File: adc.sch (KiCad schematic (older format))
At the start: 86 parts, among them J1 Conn_02x08_Odd_Even, J2 Conn_02x08_Odd_Even, J3 Conn_02x08_Odd_Even, J4 Conn_02x08_Odd_Even, J5 Conn_01x04_Male, J9 Conn_02x08_Odd_Even, U1 ADC128D818, U2 ADC128D818, U3 ADC128D818, U4 ADC128D818, U5 ADC128D818

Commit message: change tantalum cap footprint to Kemet C
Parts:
- C1, C10, C2, C5, C7, C9: footprint Capacitor_Tantalum_SMD:CP_EIA-3216-18_Kemet-A_Pad1.58x1.35mm_HandSolder -> Capacitor_Tantalum_SMD:CP_EIA-6032-28_Kemet-C_Pad2.25x2.35mm_HandSolder
- C13, C15, C17, C19: footprint Capacitor_Tantalum_SMD:CP_EIA-3528-12_Kemet-T_Pad1.50x2.35mm_HandSolder -> Capacitor_Tantalum_SMD:CP_EIA-6032-28_Kemet-C_Pad2.25x2.35mm_HandSolder
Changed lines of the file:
@@
 F 0 "C13" V 6650 5700 50  0000 L CNN
 F 1 "1U TANT C" V 6550 5400 50  0000 L CNN
-F 2 "Capacitor_Tantalum_SMD:CP_EIA-3528-12_Kemet-T_Pad1.50x2.35mm_HandSolder" H 6588 5900 50  0001 C CNN
+F 2 "Capacitor_Tantalum_SMD:CP_EIA-6032-28_Kemet-C_Pad2.25x2.35mm_HandSolder" H 6588 5900 50  0001 C CNN
 F 3 "~" H 6550 6050 50  0001 C CNN
 	1    6550 6050
@@
 F 0 "C9" H 4450 4300 50  0000 L CNN
 F 1 "1U TANT C" H 4400 4200 50  0000 L CNN
-F 2 "Capacitor_Tantalum_SMD:CP_EIA-3216-18_Kemet-A_Pad1.58x1.35mm_HandSolder" H 4938 4100 50  0001 C CNN
+F 2 "Capacitor_Tantalum_SMD:CP_EIA-6032-28_Kemet-C_Pad2.25x2.35mm_HandSolder" H 4938 4100 50  0001 C CNN
 F 3 "~" H 4900 4250 50  0001 C CNN
 	1    4900 4250
@@
 F 0 "C5" V 3100 6300 50  0000 L CNN
 F 1 "1U TANT C" V 3000 6000 50  0000 L CNN
-F 2 "Capacitor_Tantalum_SMD:CP_EIA-3216-18_Kemet-A_Pad1.58x1.35mm_HandSolder" H 3038 6500 50  0001 C CNN
+F 2 "Capacitor_Tantalum_SMD:CP_EIA-6032-28_Kemet-C_Pad2.25x2.35mm_HandSolder" H 3038 6500 50  0001 C CNN
 F 3 "~" H 3000 6650 50  0001 C CNN
 	1    3000 6650
@@
 F 0 "C1" H 900 4900 50  0000 L CNN
 F 1 "1U TANT C" H 850 4800 50  0000 L CNN
-F 2 "Capacitor_Tantalum_SMD:CP_EIA-3216-18_Kemet-A_Pad1.58x1.35mm_HandSolder" H 1388 4700 50  0001 C CNN
+F 2 "Capacitor_Tantalum_SMD:CP_EIA-6032-28_Kemet-C_Pad2.25x2.35mm_HandSolder" H 1388 4700 50  0001 C CNN
 F 3 "~" H 1350 4850 50  0001 C CNN
 	1    1350 4850
@@
 F 0 "C7" V 3500 2800 50  0000 L CNN
 F 1 "1U TANT C" V 3400 2500 50  0000 L CNN
-F 2 "Capacitor_Tantalum_SMD:CP_EIA-3216-18_Kemet-A_Pad1.58x1.35mm_HandSolder" H 3438 3000 50  0001 C CNN
+F 2 "Capacitor_Tantalum_SMD:CP_EIA-6032-28_Kemet-C_Pad2.25x2.35mm_HandSolder" H 3438 3000 50  0001 C CNN
 F 3 "~" H 3400 3150 50  0001 C CNN
 	1    3400 3150
@@
 F 0 "C2" H 1300 1400 50  0000 L CNN
 F 1 "1U TANT C" H 1250 1300 50  0000 L CNN
-F 2 "Capacitor_Tantalum_SMD:CP_EIA-3216-18_Kemet-A_Pad1.58x1.35mm_HandSolder" H 1788 1200 50  0001 C CNN
+F 2 "Capacitor_Tantalum_SMD:CP_EIA-6032-28_Kemet-C_Pad2.25x2.35mm_HandSolder" H 1788 1200 50  0001 C CNN
 F 3 "~" H 1750 1350 50  0001 C CNN
 	1    1750 1350
@@
 F 0 "C19" V 10200 2600 50  0000 L CNN
 F 1 "1U TANT C" V 10100 2300 50  0000 L CNN
-F 2 "Capacitor_Tantalum_SMD:CP_EIA-3528-12_Kemet-T_Pad1.50x2.35mm_HandSolder" H 10138 2800 50  0001 C CNN
+F 2 "Capacitor_Tantalum_SMD:CP_EIA-6032-28_Kemet-C_Pad2.25x2.35mm_HandSolder" H 10138 2800 50  0001 C CNN
 F 3 "~" H 10100 2950 50  0001 C CNN
 	1    10100 2950
@@
 F 0 "C17" H 8000 1200 50  0000 L CNN
 F 1 "1U TANT C" H 7950 1100 50  0000 L CNN
-F 2 "Capacitor_Tantalum_SMD:CP_EIA-3528-12_Kemet-T_Pad1.50x2.35mm_HandSolder" H 8488 1000 50  0001 C CNN
+F 2 "Capacitor_Tantalum_SMD:CP_EIA-6032-28_Kemet-C_Pad2.25x2.35mm_HandSolder" H 8488 1000 50  0001 C CNN
 F 3 "~" H 8450 1150 50  0001 C CNN
 	1    8450 1150
@@
 F 0 "C15" V 6950 2600 50  0000 L CNN
 F 1 "1U TANT C" V 6850 2300 50  0000 L CNN
-F 2 "Capacitor_Tantalum_SMD:CP_EIA-3528-12_Kemet-T_Pad1.50x2.35mm_HandSolder" H 6888 2800 50  0001 C CNN
+F 2 "Capacitor_Tantalum_SMD:CP_EIA-6032-28_Kemet-C_Pad2.25x2.35mm_HandSolder" H 6888 2800 50  0001 C CNN
 F 3 "~" H 6850 2950 50  0001 C CNN
 	1    6850 2950
@@
 F 0 "C10" H 4750 1200 50  0000 L CNN
 F 1 "1U TANT C" H 4700 1100 50  0000 L CNN
-F 2 "Capacitor_Tantalum_SMD:CP_EIA-3216-18_Kemet-A_Pad1.58x1.35mm_HandSolder" H 5238 1000 50  0001 C CNN
+F 2 "Capacitor_Tantalum_SMD:CP_EIA-6032-28_Kemet-C_Pad2.25x2.35mm_HandSolder" H 5238 1000 50  0001 C CNN
 F 3 "~" H 5200 1150 50  0001 C CNN
 	1    5200 1150

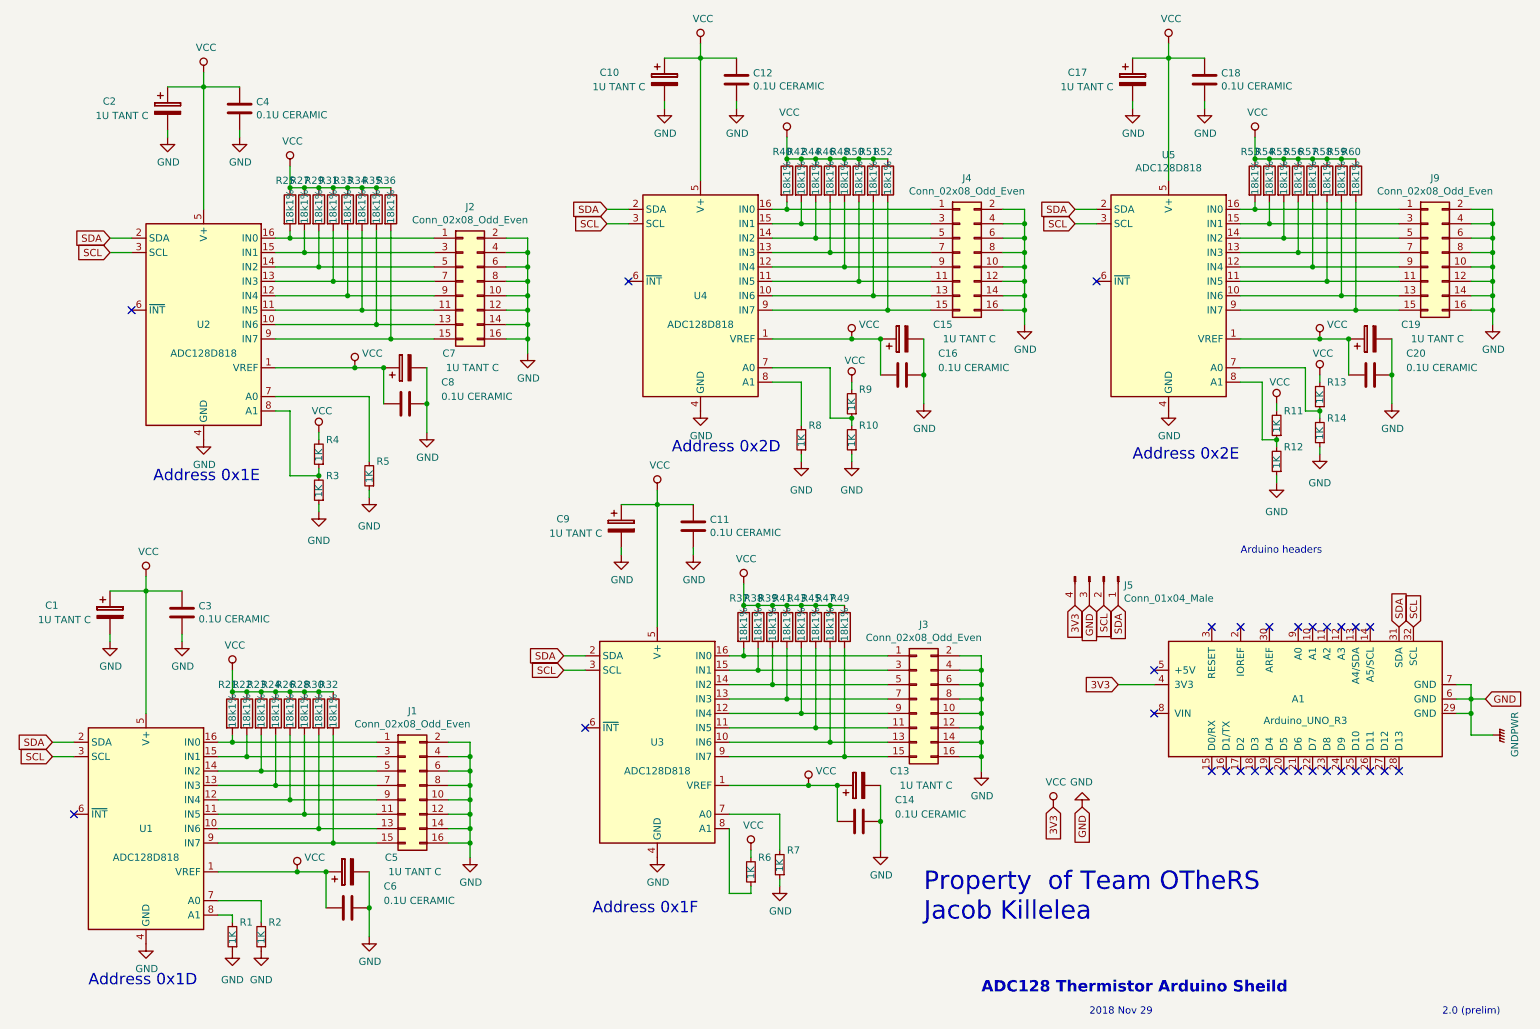
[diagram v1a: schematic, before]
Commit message: Replaced female 2x8 headers with male. Female makes more sense on the thermistors
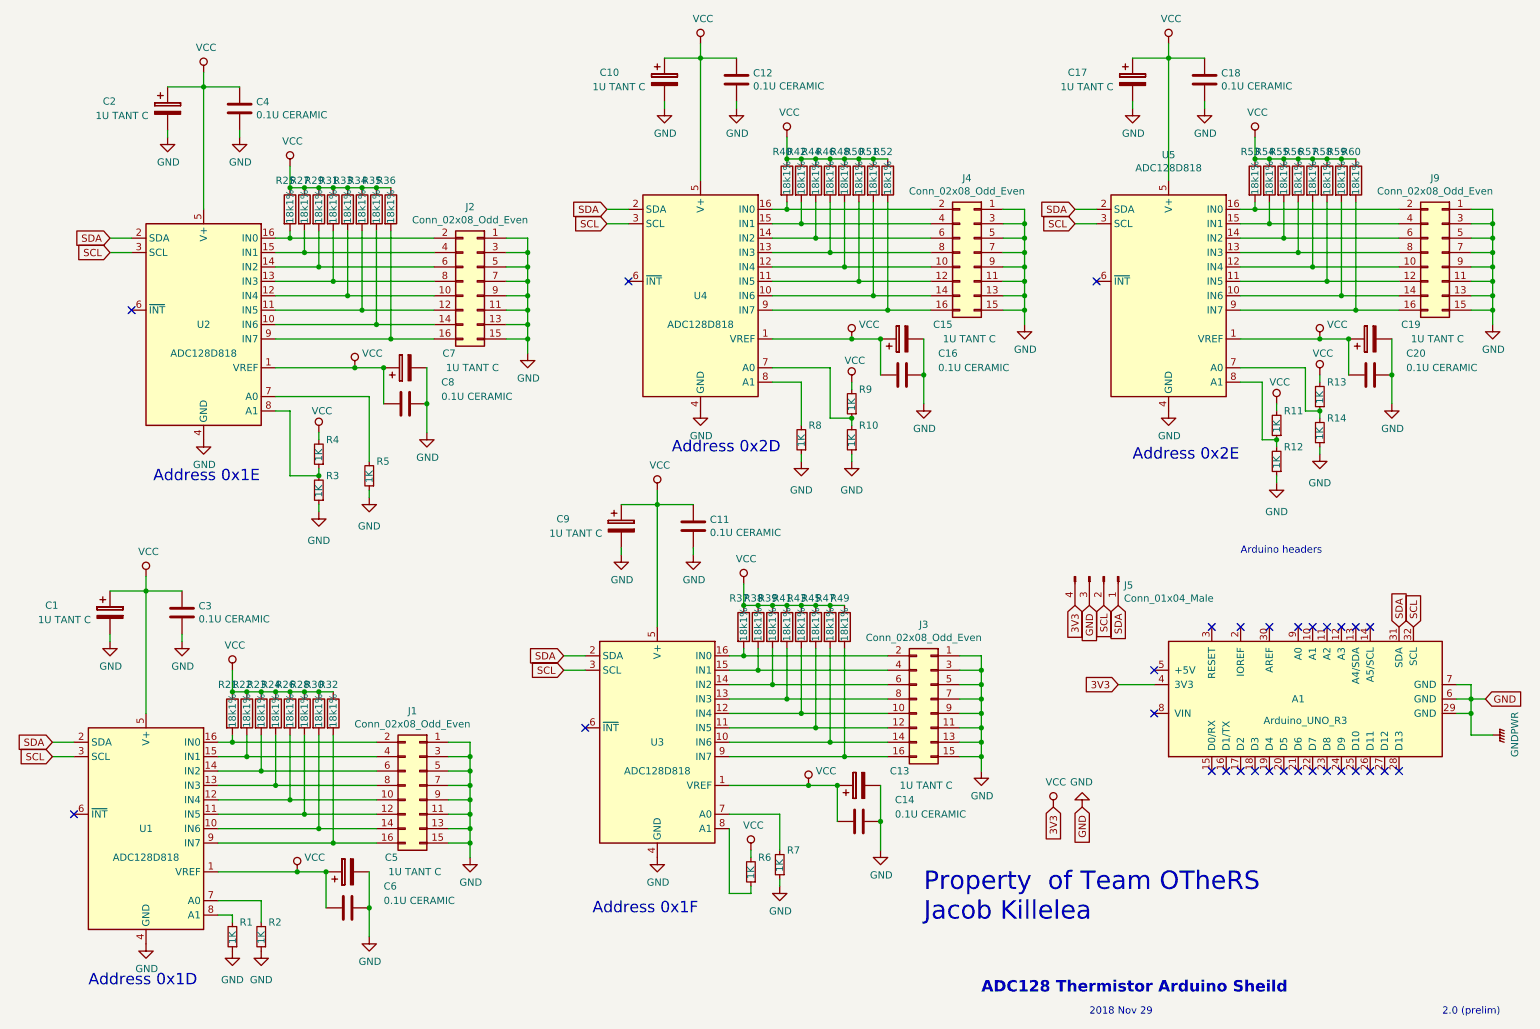
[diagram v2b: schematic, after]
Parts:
- J1, J2, J3, J4, J9: footprint Connector_PinSocket_2.54mm:PinSocket_2x08_P2.54mm_Vertical -> Connector_PinHeader_2.54mm:PinHeader_2x08_P2.54mm_Vertical
- J5: footprint Connector_PinSocket_2.54mm:PinSocket_1x04_P2.54mm_Vertical -> Connector_PinHeader_2.54mm:PinHeader_1x04_P2.54mm_Vertical
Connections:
- net GND: now also J1.1 (Pin_1), J1.11 (Pin_11), J1.13 (Pin_13), J1.15 (Pin_15), J1.3 (Pin_3), J1.5 (Pin_5), J1.7 (Pin_7), J1.9 (Pin_9), J2.1 (Pin_1), J2.11 (Pin_11), J2.13 (Pin_13), J2.15 (Pin_15), J2.3 (Pin_3), J2.5 (Pin_5), J2.7 (Pin_7), J2.9 (Pin_9), J3.1 (Pin_1), J3.11 (Pin_11), J3.13 (Pin_13), J3.15 (Pin_15), J3.3 (Pin_3), J3.5 (Pin_5), J3.7 (Pin_7), J3.9 (Pin_9), J4.1 (Pin_1), J4.11 (Pin_11), J4.13 (Pin_13), J4.15 (Pin_15), J4.3 (Pin_3), J4.5 (Pin_5), J4.7 (Pin_7), J4.9 (Pin_9), J9.1 (Pin_1), J9.11 (Pin_11), J9.13 (Pin_13), J9.15 (Pin_15), J9.3 (Pin_3), J9.5 (Pin_5), J9.7 (Pin_7), J9.9 (Pin_9); no longer J1.10 (Pin_10), J1.12 (Pin_12), J1.14 (Pin_14), J1.16 (Pin_16), J1.2 (Pin_2), J1.4 (Pin_4), J1.6 (Pin_6), J1.8 (Pin_8), J2.10 (Pin_10), J2.12 (Pin_12), J2.14 (Pin_14), J2.16 (Pin_16), J2.2 (Pin_2), J2.4 (Pin_4), J2.6 (Pin_6), J2.8 (Pin_8), J3.10 (Pin_10), J3.12 (Pin_12), J3.14 (Pin_14), J3.16 (Pin_16), J3.2 (Pin_2), J3.4 (Pin_4), J3.6 (Pin_6), J3.8 (Pin_8), J4.10 (Pin_10), J4.12 (Pin_12), J4.14 (Pin_14), J4.16 (Pin_16), J4.2 (Pin_2), J4.4 (Pin_4), J4.6 (Pin_6), J4.8 (Pin_8), J9.10 (Pin_10), J9.12 (Pin_12), J9.14 (Pin_14), J9.16 (Pin_16), J9.2 (Pin_2), J9.4 (Pin_4), J9.6 (Pin_6), J9.8 (Pin_8)
- net at R47.2, U3.10 (IN6): now also J3.14 (Pin_14); no longer J3.13 (Pin_13)
- net at R45.2, U3.11 (IN5): now also J3.12 (Pin_12); no longer J3.11 (Pin_11)
- net at R43.2, U3.12 (IN4): now also J3.10 (Pin_10); no longer J3.9 (Pin_9)
- net at R41.2, U3.13 (IN3): now also J3.8 (Pin_8); no longer J3.7 (Pin_7)
- net at R39.2, U3.14 (IN2): now also J3.6 (Pin_6); no longer J3.5 (Pin_5)
- net at R38.2, U3.15 (IN1): now also J3.4 (Pin_4); no longer J3.3 (Pin_3)
- net at R37.2, U3.16 (IN0): now also J3.2 (Pin_2); no longer J3.1 (Pin_1)
- net at R49.2, U3.9 (IN7): now also J3.16 (Pin_16); no longer J3.15 (Pin_15)
- net at R30.2, U1.10 (IN6): now also J1.14 (Pin_14); no longer J1.13 (Pin_13)
- net at R28.2, U1.11 (IN5): now also J1.12 (Pin_12); no longer J1.11 (Pin_11)
- net at R26.2, U1.12 (IN4): now also J1.10 (Pin_10); no longer J1.9 (Pin_9)
- net at R24.2, U1.13 (IN3): now also J1.8 (Pin_8); no longer J1.7 (Pin_7)
- net at R23.2, U1.14 (IN2): now also J1.6 (Pin_6); no longer J1.5 (Pin_5)
- net at R22.2, U1.15 (IN1): now also J1.4 (Pin_4); no longer J1.3 (Pin_3)
- net at R21.2, U1.16 (IN0): now also J1.2 (Pin_2); no longer J1.1 (Pin_1)
- net at R32.2, U1.9 (IN7): now also J1.16 (Pin_16); no longer J1.15 (Pin_15)
- net at R35.2, U2.10 (IN6): now also J2.14 (Pin_14); no longer J2.13 (Pin_13)
- net at R34.2, U2.11 (IN5): now also J2.12 (Pin_12); no longer J2.11 (Pin_11)
- net at R33.2, U2.12 (IN4): now also J2.10 (Pin_10); no longer J2.9 (Pin_9)
- net at R31.2, U2.13 (IN3): now also J2.8 (Pin_8); no longer J2.7 (Pin_7)
- net at R29.2, U2.14 (IN2): now also J2.6 (Pin_6); no longer J2.5 (Pin_5)
- net at R27.2, U2.15 (IN1): now also J2.4 (Pin_4); no longer J2.3 (Pin_3)
- net at R25.2, U2.16 (IN0): now also J2.2 (Pin_2); no longer J2.1 (Pin_1)
- net at R36.2, U2.9 (IN7): now also J2.16 (Pin_16); no longer J2.15 (Pin_15)
- net at R59.2, U5.10 (IN6): now also J9.14 (Pin_14); no longer J9.13 (Pin_13)
- net at R58.2, U5.11 (IN5): now also J9.12 (Pin_12); no longer J9.11 (Pin_11)
- net at R57.2, U5.12 (IN4): now also J9.10 (Pin_10); no longer J9.9 (Pin_9)
- net at R56.2, U5.13 (IN3): now also J9.8 (Pin_8); no longer J9.7 (Pin_7)
- net at R55.2, U5.14 (IN2): now also J9.6 (Pin_6); no longer J9.5 (Pin_5)
- net at R54.2, U5.15 (IN1): now also J9.4 (Pin_4); no longer J9.3 (Pin_3)
- net at R53.2, U5.16 (IN0): now also J9.2 (Pin_2); no longer J9.1 (Pin_1)
- net at R60.2, U5.9 (IN7): now also J9.16 (Pin_16); no longer J9.15 (Pin_15)
- net at R51.2, U4.10 (IN6): now also J4.14 (Pin_14); no longer J4.13 (Pin_13)
- net at R50.2, U4.11 (IN5): now also J4.12 (Pin_12); no longer J4.11 (Pin_11)
- net at R48.2, U4.12 (IN4): now also J4.10 (Pin_10); no longer J4.9 (Pin_9)
- net at R46.2, U4.13 (IN3): now also J4.8 (Pin_8); no longer J4.7 (Pin_7)
- net at R44.2, U4.14 (IN2): now also J4.6 (Pin_6); no longer J4.5 (Pin_5)
- net at R42.2, U4.15 (IN1): now also J4.4 (Pin_4); no longer J4.3 (Pin_3)
- net at R40.2, U4.16 (IN0): now also J4.2 (Pin_2); no longer J4.1 (Pin_1)
- net at R52.2, U4.9 (IN7): now also J4.16 (Pin_16); no longer J4.15 (Pin_15)
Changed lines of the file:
@@
 L Connector_Generic:Conn_02x08_Odd_Even J3
 U 1 1 5C07D8AC
-P 6950 5450
-F 0 "J3" H 7000 5967 50  0000 C CNN
-F 1 "Conn_02x08_Odd_Even" H 7000 5876 50  0000 C CNN
-F 2 "Connector_PinSocket_2.54mm:PinSocket_2x08_P2.54mm_Vertical" H 6950 5450 50  0001 C CNN
-F 3 "~" H 6950 5450 50  0001 C CNN
-	1    6950 5450
-	1    0    0    -1
+P 7050 5450
+F 0 "J3" H 7100 5967 50  0000 C CNN
+F 1 "Conn_02x08_Odd_Even" H 7100 5876 50  0000 C CNN
+F 2 "Connector_PinHeader_2.54mm:PinHeader_2x08_P2.54mm_Vertical" H 7050 5450 50  0001 C CNN
+F 3 "~" H 7050 5450 50  0001 C CNN
+	1    7050 5450
+	-1   0    0    -1
 $EndComp
 Text Notes 9200 4450 0    50   ~ 0
@@
 L Connector_Generic:Conn_02x08_Odd_Even J1
 U 1 1 5C17FACF
-P 3400 6050
-F 0 "J1" H 3450 6567 50  0000 C CNN
-F 1 "Conn_02x08_Odd_Even" H 3450 6476 50  0000 C CNN
-F 2 "Connector_PinSocket_2.54mm:PinSocket_2x08_P2.54mm_Vertical" H 3400 6050 50  0001 C CNN
-F 3 "~" H 3400 6050 50  0001 C CNN
-	1    3400 6050
-	1    0    0    -1
+P 3500 6050
+F 0 "J1" H 3550 6567 50  0000 C CNN
+F 1 "Conn_02x08_Odd_Even" H 3550 6476 50  0000 C CNN
+F 2 "Connector_PinHeader_2.54mm:PinHeader_2x08_P2.54mm_Vertical" H 3500 6050 50  0001 C CNN
+F 3 "~" H 3500 6050 50  0001 C CNN
+	1    3500 6050
+	-1   0    0    -1
 $EndComp
 Wire Wire Line
@@
 L Connector_Generic:Conn_02x08_Odd_Even J2
 U 1 1 5C1842E3
-P 3800 2550
-F 0 "J2" H 3850 3067 50  0000 C CNN
-F 1 "Conn_02x08_Odd_Even" H 3850 2976 50  0000 C CNN
-F 2 "Connector_PinSocket_2.54mm:PinSocket_2x08_P2.54mm_Vertical" H 3800 2550 50  0001 C CNN
-F 3 "~" H 3800 2550 50  0001 C CNN
-	1    3800 2550
-	1    0    0    -1
+P 3900 2550
+F 0 "J2" H 3950 3067 50  0000 C CNN
+F 1 "Conn_02x08_Odd_Even" H 3950 2976 50  0000 C CNN
+F 2 "Connector_PinHeader_2.54mm:PinHeader_2x08_P2.54mm_Vertical" H 3900 2550 50  0001 C CNN
+F 3 "~" H 3900 2550 50  0001 C CNN
+	1    3900 2550
+	-1   0    0    -1
 $EndComp
 Wire Wire Line
@@
 L Connector_Generic:Conn_02x08_Odd_Even J9
 U 1 1 5C18D11C
-P 10500 2350
-F 0 "J9" H 10550 2867 50  0000 C CNN
-F 1 "Conn_02x08_Odd_Even" H 10550 2776 50  0000 C CNN
-F 2 "Connector_PinSocket_2.54mm:PinSocket_2x08_P2.54mm_Vertical" H 10500 2350 50  0001 C CNN
-F 3 "~" H 10500 2350 50  0001 C CNN
-	1    10500 2350
-	1    0    0    -1
+P 10600 2350
+F 0 "J9" H 10650 2867 50  0000 C CNN
+F 1 "Conn_02x08_Odd_Even" H 10650 2776 50  0000 C CNN
+F 2 "Connector_PinHeader_2.54mm:PinHeader_2x08_P2.54mm_Vertical" H 10600 2350 50  0001 C CNN
+F 3 "~" H 10600 2350 50  0001 C CNN
+	1    10600 2350
+	-1   0    0    -1
 $EndComp
 Wire Wire Line
@@
 L Connector_Generic:Conn_02x08_Odd_Even J4
 U 1 1 5C19E827
-P 7250 2350
-F 0 "J4" H 7300 2867 50  0000 C CNN
-F 1 "Conn_02x08_Odd_Even" H 7300 2776 50  0000 C CNN
-F 2 "Connector_PinSocket_2.54mm:PinSocket_2x08_P2.54mm_Vertical" H 7250 2350 50  0001 C CNN
-F 3 "~" H 7250 2350 50  0001 C CNN
-	1    7250 2350
-	1    0    0    -1
+P 7350 2350
+F 0 "J4" H 7400 2867 50  0000 C CNN
+F 1 "Conn_02x08_Odd_Even" H 7400 2776 50  0000 C CNN
+F 2 "Connector_PinHeader_2.54mm:PinHeader_2x08_P2.54mm_Vertical" H 7350 2350 50  0001 C CNN
+F 3 "~" H 7350 2350 50  0001 C CNN
+	1    7350 2350
+	-1   0    0    -1
 $EndComp
 Wire Wire Line
@@
 F 0 "J5" V 8310 4740 50  0000 L CNN
 F 1 "Conn_01x04_Male" V 8401 4740 50  0000 L CNN
-F 2 "Connector_PinSocket_2.54mm:PinSocket_1x04_P2.54mm_Vertical" H 8250 4600 50  0001 C CNN
+F 2 "Connector_PinHeader_2.54mm:PinHeader_1x04_P2.54mm_Vertical" H 8250 4600 50  0001 C CNN
 F 3 "~" H 8250 4600 50  0001 C CNN
 	1    8250 4600
